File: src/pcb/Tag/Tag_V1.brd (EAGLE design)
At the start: 68.6 x 44.5 mm, 28 parts, among them IC1 ATMEGA328P-AU, IC2 DWM1000, IC3 MIC5219-3.3YM5-TR, J1 AVR_SPI_PROG_3X2PTH, Q1 8MHz

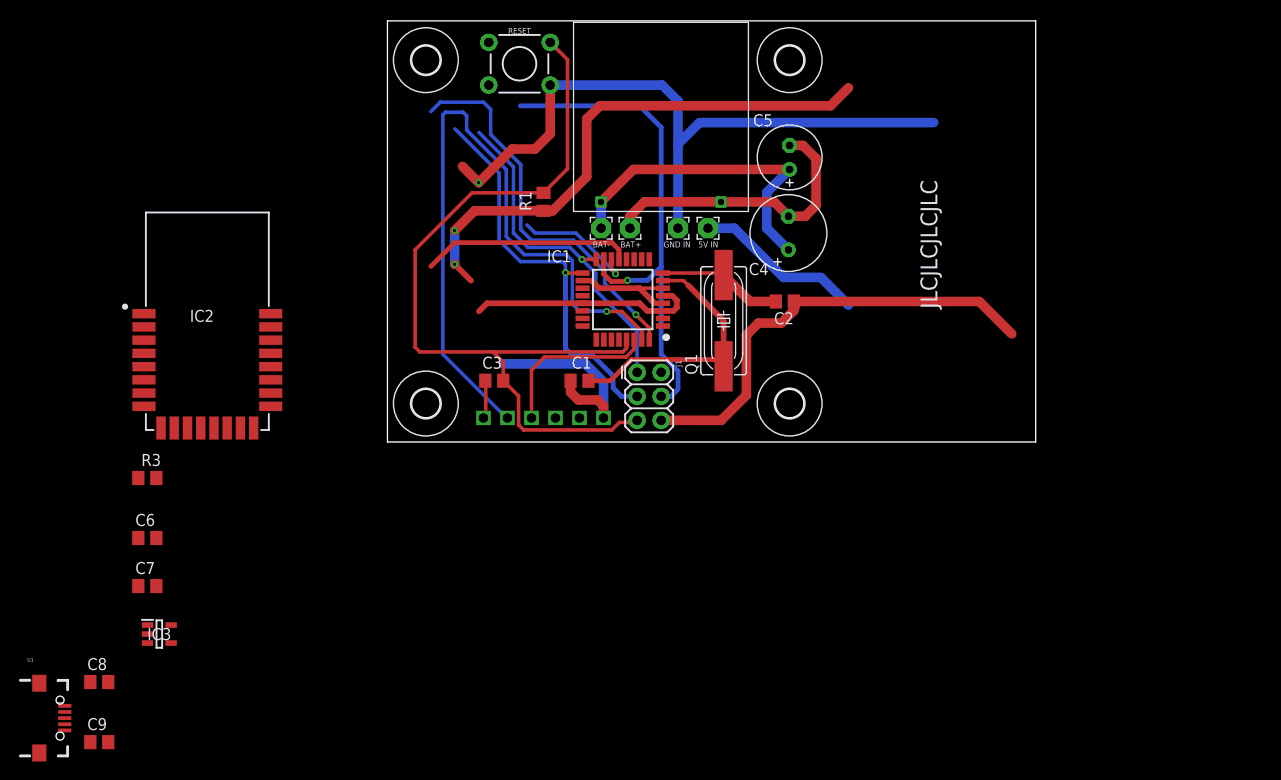
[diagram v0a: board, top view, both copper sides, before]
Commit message: Final version V1 tag
-Uses MIC5219 to convert 5V to 3.3V
-DWM module is now soldered on the PCB
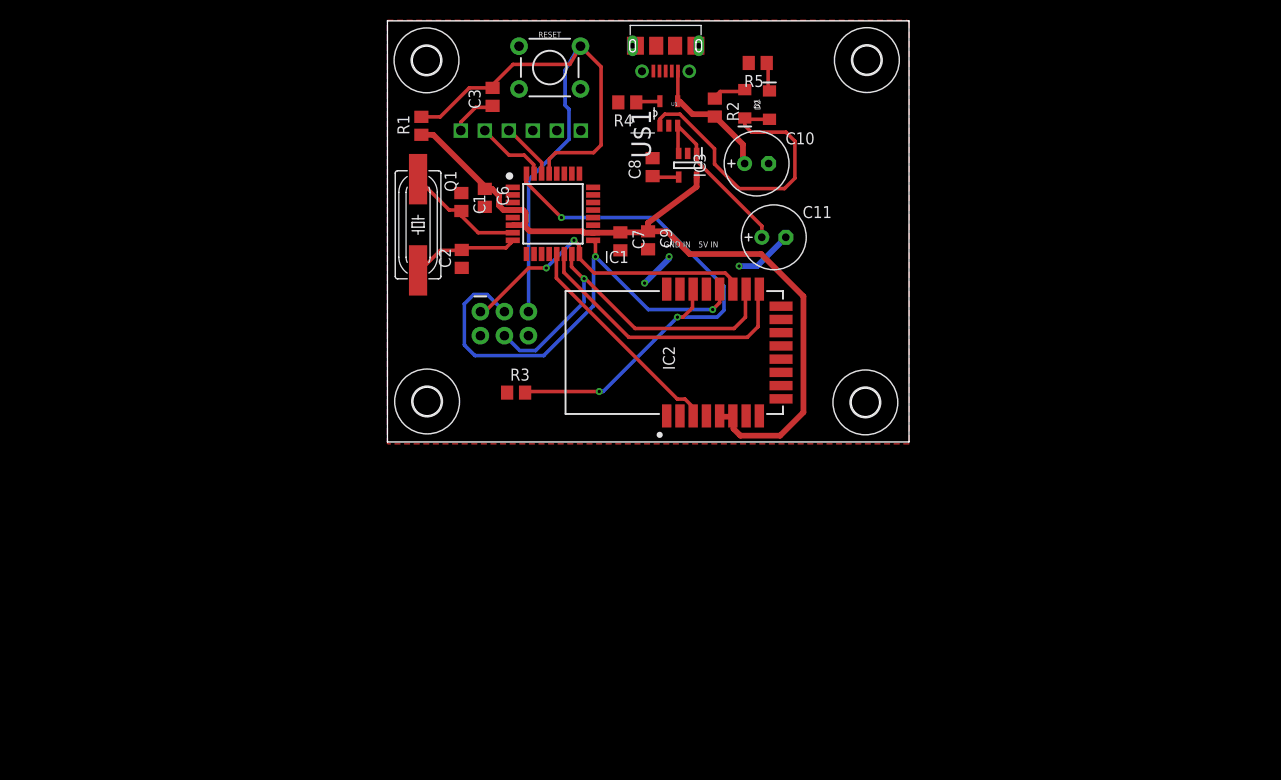
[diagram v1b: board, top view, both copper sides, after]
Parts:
- removed 5V-IN, BAT+, BAT-: (no value), wirepad:2,15/1,0
- removed C4: 100uF, rcl:E3,5-8
- removed C5: 10uF, rcl:E2,5-7
- removed GND-IN: GND_IN, wirepad:2,15/1,0
- removed U$4: 18650-CHARGE-5V-OUT, Eigen Library:18650-CHARGE-5V-OUT
- added C10, C11: 10uF, rcl:E2,5-7
- added D1: RED, SparkFun-LED:LED-1206
- added D2: GREEN, SparkFun-LED:LED-1206
- added R2, R5: 470, rcl:R0805
- added R4: 2k2, rcl:R0805
- added U$1: MCP73831T-2ACI/OT, MCP73831T-2ACI_OT:SOT95P280X145-5N
- U1: value (none) -> 105017-0001; device MicroUSB:USB-MICRO-SMD -> 105017-0001:MOLEX_105017-0001
- moved U1 97.2 mm to (29.4, 41.9), turned to 180 degrees
- moved C8 80.0 mm to (28.1, 29.1), turned to 90 degrees
- moved C9 78.7 mm to (27.6, 21.3), turned to 270 degrees
- moved IC3 74.7 mm to (31.8, 29.3), turned to 270 degrees
- moved C7 61.9 mm to (24.6, 21.2), turned to 270 degrees
- moved IC2 61.4 mm to (41.8, 9.46), turned to 90 degrees
- moved H1 59.1 mm to (50.7, 40.4)
- moved C6 50.7 mm to (10.3, 25.8), turned to 270 degrees
- moved R3 40.0 mm to (13.6, 5.22)
- moved H3 38.4 mm to (4.20, 4.28)
- moved H4 37.1 mm to (50.6, 4.19)
- moved C2 34.5 mm to (7.86, 19.4), turned to 270 degrees
- moved Q1 33.9 mm to (3.24, 23.0), turned to 270 degrees
- moved U$2 30.5 mm to (20.5, 32.9)
- moved C3 30.0 mm to (11.1, 36.5), turned to 90 degrees
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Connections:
- new net BAT+: C11.+, IC3.1, IC3.3, U$1.3
- new net N$6: R4.1, U$1.5
- net 5V: now also C10.+, R2.2, U$1.4, U1.1; no longer 5V-IN.1
- net GND: now also C10.-, C11.-, R4.2, R5.2, U$1.2, U1.5; no longer GND-IN.1
- net N$1: now also D1.C, D2.A, U$1.1; no longer BAT-.1, C4.+, C5.+, U$4.B-
- net N$2: now also D1.A, R2.1; no longer BAT+.1, C4.-, C5.-, U$4.B+
- net N$4: now also D2.C, R5.1; no longer IC3.1, IC3.3
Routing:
- net GND: track 166.9 -> 10.1 mm, vias 1 -> 3
- net TX: track 74.3 -> 7.63 mm, vias 1 -> 0
- net N$2: track 31.0 -> 3.65 mm
- net RESET: track 89.9 -> 70.1 mm
- net BAT+: track 0.00 -> 18.5 mm
- net IRQ: track 41.0 -> 57.6 mm, vias 1 -> 3
- net CS: track 13.3 -> 29.8 mm, vias 1 -> 0
- net XTAL1: track 28.5 -> 12.7 mm
- net 3.3V: track 68.6 -> 84.1 mm, vias 2 -> 0
- net MOSI: track 55.0 -> 39.6 mm
- net RX: track 17.8 -> 6.04 mm
- net SCK: track 42.9 -> 50.4 mm, vias 1 -> 2
- net 5V: track 18.2 -> 14.1 mm
- net MISO: track 36.4 -> 33.3 mm, vias 1 -> 2
- net N$4: track 0.00 -> 3.09 mm
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- added copper zone on layer 1, net GND
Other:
- board size 68.6 x 44.5 mm -> 55.2 x 44.5 mm
- board text removed: "JLCJLCJLCJLC"

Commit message: Added gerber files
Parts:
- moved H3 1.35 mm to (5.25, 5.13)
- moved H1 0.86 mm to (50.0, 39.9)
- moved H4 0.68 mm to (50.2, 4.74)
- moved H2 0.49 mm to (4.58, 40.2)
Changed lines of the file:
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@@
 <attribute name="SPICEPREFIX" value="C" x="79.703" y="92.383" size="1.778" layer="27" rot="R90" display="off"/>
 </element>
-<element name="H1" library="holes" library_urn="urn:adsk.eagle:library:237" package="3,0" package3d_urn="urn:adsk.eagle:package:14277/1" value="MOUNT-HOLE3.0" x="50.714" y="40.394" smashed="yes"/>
-<element name="H2" library="holes" library_urn="urn:adsk.eagle:library:237" package="3,0" package3d_urn="urn:adsk.eagle:package:14277/1" value="MOUNT-HOLE3.0" x="4.134" y="40.366" smashed="yes"/>
+<element name="H1" library="holes" library_urn="urn:adsk.eagle:library:237" package="3,0" package3d_urn="urn:adsk.eagle:package:14277/1" value="MOUNT-HOLE3.0" x="50.014" y="39.894" smashed="yes"/>
+<element name="H2" library="holes" library_urn="urn:adsk.eagle:library:237" package="3,0" package3d_urn="urn:adsk.eagle:package:14277/1" value="MOUNT-HOLE3.0" x="4.584" y="40.166" smashed="yes"/>
 <element name="IC1" library="ATMEGA328P-AU" package="QFP80P900X900X120-32N" value="ATMEGA328P-AU" x="17.508" y="24.132" smashed="yes">
 <attribute name="ARROW_PART_NUMBER" value="ATMEGA328P-AU" x="61.958" y="-12.698" size="1.778" layer="27" display="off"/>
@@
 </element>
 <element name="U$2" library="Eigen Library" package="UART-6PIN" value="UART-6PIN" x="20.46" y="32.94" smashed="yes" rot="R180"/>
-<element name="H3" library="holes" library_urn="urn:adsk.eagle:library:237" package="3,0" package3d_urn="urn:adsk.eagle:package:14277/1" value="MOUNT-HOLE3.0" x="4.195" y="4.284" smashed="yes"/>
-<element name="H4" library="holes" library_urn="urn:adsk.eagle:library:237" package="3,0" package3d_urn="urn:adsk.eagle:package:14277/1" value="MOUNT-HOLE3.0" x="50.555" y="4.186" smashed="yes"/>
+<element name="H3" library="holes" library_urn="urn:adsk.eagle:library:237" package="3,0" package3d_urn="urn:adsk.eagle:package:14277/1" value="MOUNT-HOLE3.0" x="5.245" y="5.134" smashed="yes"/>
+<element name="H4" library="holes" library_urn="urn:adsk.eagle:library:237" package="3,0" package3d_urn="urn:adsk.eagle:package:14277/1" value="MOUNT-HOLE3.0" x="50.155" y="4.736" smashed="yes"/>
 <element name="IC2" library="DWM1000" package="DWM1000" value="DWM1000" x="41.84" y="9.46" smashed="yes" rot="R90">
 <attribute name="ARROW_PART_NUMBER" value="DWM1000" x="41.84" y="9.46" size="1.778" layer="27" rot="R90" display="off"/>

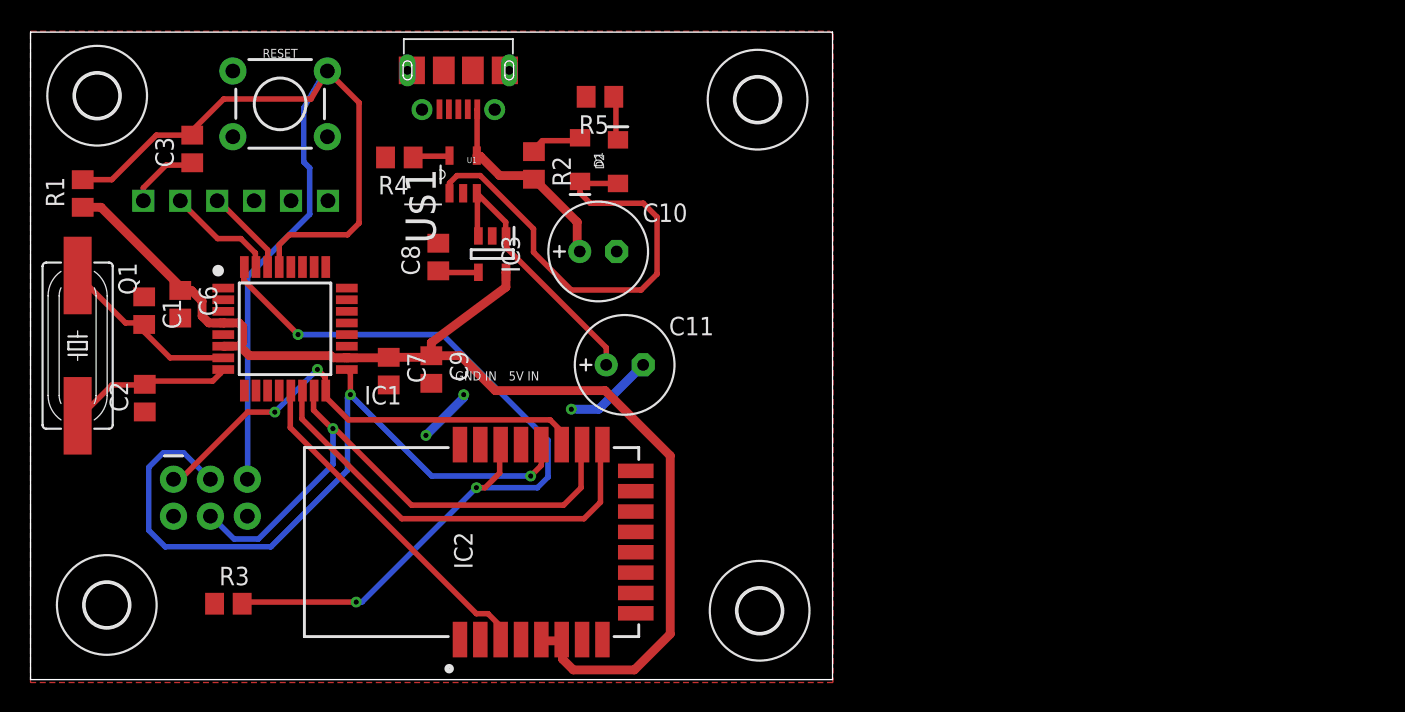
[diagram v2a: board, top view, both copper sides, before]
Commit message: Versie 2 tag batterijen op PCB
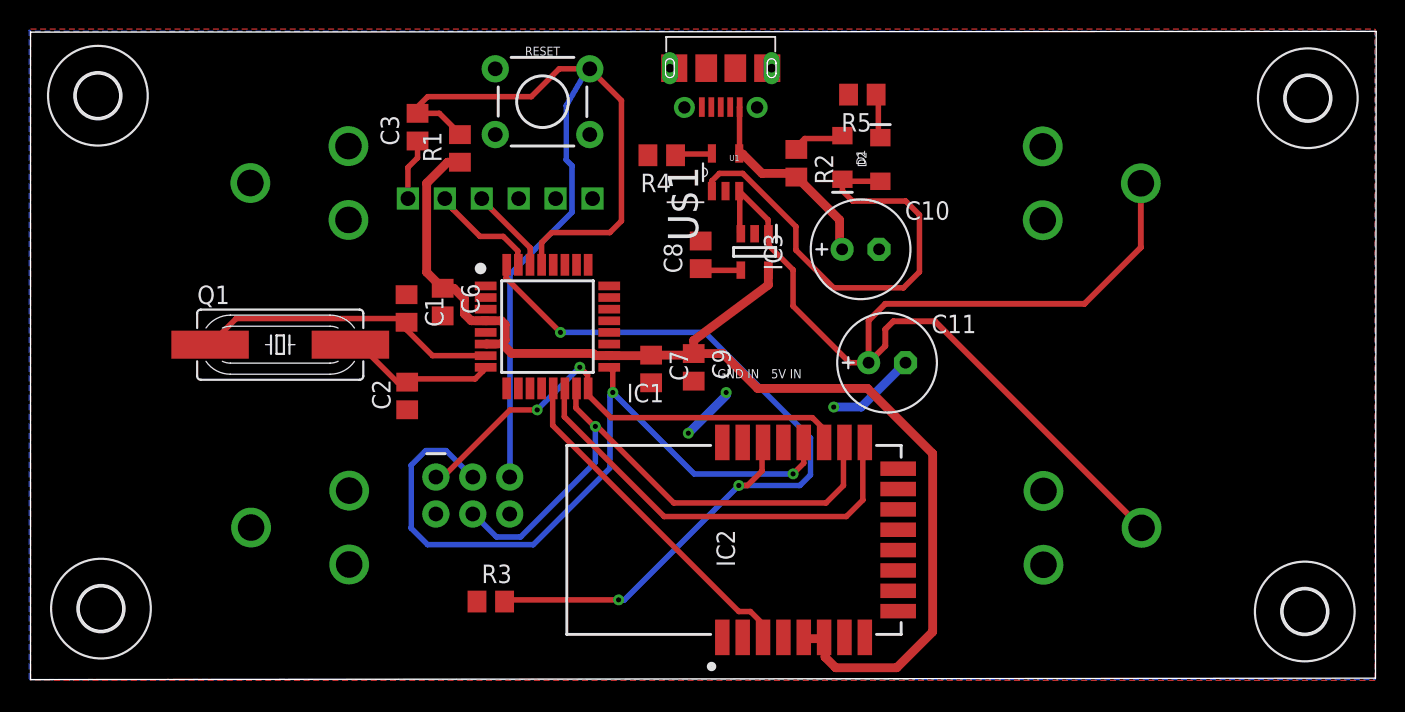
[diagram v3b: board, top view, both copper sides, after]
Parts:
- added BT1, BT2: (no value), SparkFun-Batteries:BATTERY_18650-HOLDER
- moved H1 37.9 mm to (87.9, 40.0)
- moved H4 37.5 mm to (87.7, 4.69)
- moved R1 26.1 mm to (29.5, 36.5)
- moved U$2 18.2 mm to (38.7, 33.1)
- moved C10 18.1 mm to (57.1, 29.6)
- moved C11 18.1 mm to (58.9, 21.8)
- moved D1 18.1 mm to (55.9, 35.9)
- moved D2 18.1 mm to (58.5, 35.8)
- moved C1 18.1 mm to (25.9, 25.5)
- moved C6 18.1 mm to (28.4, 26.0)
- moved C8 18.1 mm to (46.1, 29.2)
- moved IC1 18.1 mm to (35.6, 24.3)
- moved IC3 18.1 mm to (49.8, 29.4)
- moved J1 18.1 mm to (27.9, 13.9)
- moved R3 18.1 mm to (31.7, 5.37)
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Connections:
- net BAT+: now also BT1.PWR@1, BT2.PWR@1
- net GND: now also BT1.GND@1, BT2.GND@1
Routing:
- net BAT+: track 18.5 -> 73.9 mm
- net XTAL1: track 12.7 -> 21.2 mm
- net RESET: track 70.1 -> 66.6 mm
- net 3.3V: track 84.1 -> 85.5 mm
- net DTR: track 4.97 -> 4.24 mm
- added copper zone on layer 16, net GND
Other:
- board size 55.2 x 44.5 mm -> 92.6 x 44.6 mm
